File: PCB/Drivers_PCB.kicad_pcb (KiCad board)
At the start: 4 copper layers, 54 x 51 mm, 30 parts, among them J1 Power_Connector, J10 Conn_01x08, J2 Fan_Connector, J3 Motor_1_connector, J4 EOC_Switch_Connector, J5 Motor_2_connector, J6 IR_LED_Connector, J7 Conn_01x08, J8 Conn_01x06, J9 Conn_01x10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

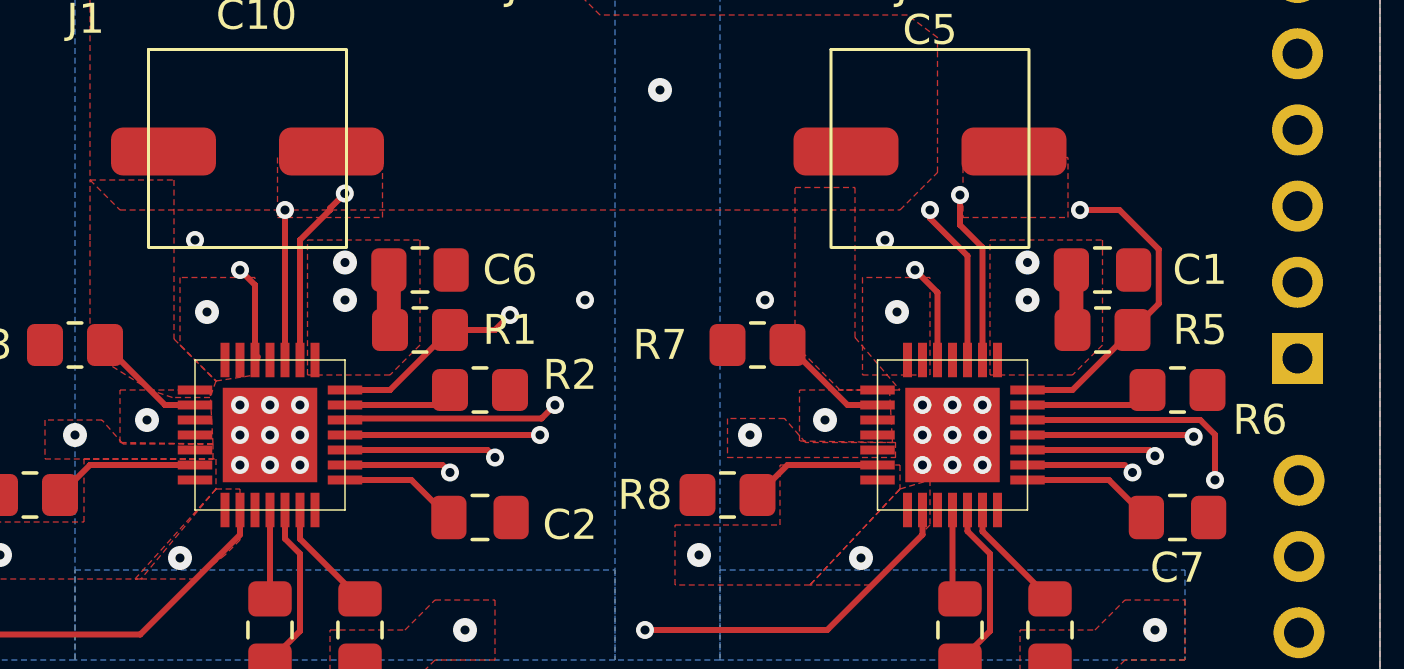
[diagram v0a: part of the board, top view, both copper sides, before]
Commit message: Fixing the shield pins matching
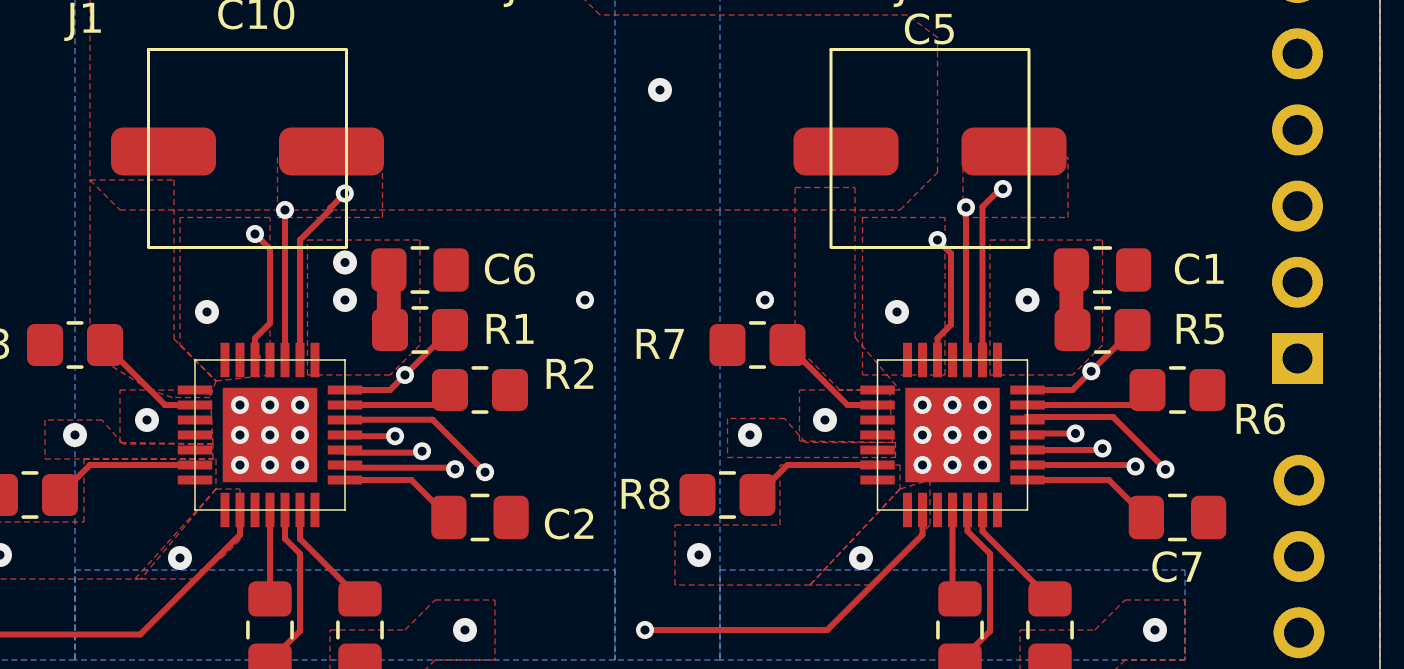
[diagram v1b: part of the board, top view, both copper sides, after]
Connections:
- J10 pad 1: DIR2 -> unconnected-(J10-Pin_1-Pad1)
- J10 pad 2: DIR1 -> unconnected-(J10-Pin_2-Pad2)
- J10 pad 3: RESET2 -> SLEEP1
- J10 pad 4: RESET1 -> SLEEP2
- J10 pad 5: SLEEP2 -> RESET1
- J10 pad 6: SLEEP1 -> RESET2
- J10 pad 7: unconnected-(J10-Pin_7-Pad7) -> DIR1
- J10 pad 8: unconnected-(J10-Pin_8-Pad8) -> DIR2
- J9 pad 1: unconnected-(J9-Pin_1-Pad1) -> MS1
- J9 pad 10: MS1 -> unconnected-(J9-Pin_10-Pad10)
- J9 pad 2: unconnected-(J9-Pin_2-Pad2) -> MS2
- J9 pad 3: unconnected-(J9-Pin_3-Pad3) -> MS3
- J9 pad 4: GND -> STEP1
- J9 pad 5: STEP2 -> IR_LED
- J9 pad 6: IR_LED -> STEP2
- J9 pad 7: STEP1 -> GND
- J9 pad 8: MS3 -> unconnected-(J9-Pin_8-Pad8)
- J9 pad 9: MS2 -> unconnected-(J9-Pin_9-Pad9)
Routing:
- net RESET1: track 81.3 -> 35.8 mm
- net MS1: track 59.4 -> 38.6 mm
- net MS2: track 57.9 -> 38.2 mm
- net MS3: track 57.0 -> 38.3 mm
- net DIR2: track 37.2 -> 19.7 mm
- net DIR1: track 59.1 -> 44.6 mm
- net SLEEP2: track 30.5 -> 21.0 mm
- net RESET2: track 21.8 -> 12.7 mm
- net STEP1: track 45.0 -> 38.8 mm
- net SLEEP1: track 45.1 -> 43.6 mm
- net IR_LED: track 16.1 -> 17.2 mm
- net VREF: track 47.0 -> 47.8 mm
- net VDD: vias 4 -> 3
- net GND: vias 22 -> 20

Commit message: PCB update, Main STM code creation, UI creation
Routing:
- net VDD: vias 3 -> 2
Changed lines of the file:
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@@
-	)
-	(via
-		(at 111.5 65.25)
-		(size 0.8)
-		(drill 0.3)
-		(layers "F.Cu" "B.Cu")
-		(free yes)
-		(net 12)
 	)
 	(via

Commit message: Cleaning the git
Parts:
- added J11: SWITCH_Connector, Connector_JST:JST_XH_B2B-XH-A_1x02_P2.50mm_Vertical, F.Cu at (116.5, 52.1)
- moved J2 7.00 mm to (124.0, 51.0)
- moved J6 3.90 mm to (133.0, 51.0)
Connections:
- J1 pad 1: VBB -> Net-(J1-Pin_1)
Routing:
- net IR_LED: track 17.2 -> 15.6 mm
- net VBB: vias 7 -> 5
- added copper zone on F.Cu, net Net-(J1-Pin_1)

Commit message: finishing PCB
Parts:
- added G***: LOGO, logos:etis_logo, F.Cu at (131.5, 84.0)
- added G***: LOGO, logos:ensea_logo, F.Cu at (102.5, 82.5)
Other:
- board text added: "ARCHENAULT Maël/GEORGE Louis"
